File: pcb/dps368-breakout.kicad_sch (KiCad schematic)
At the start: 7 parts, among them J1 Conn_01x05_Pin, U1 DPS368XTSA1

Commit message: Removed broken property
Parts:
- U1:  Package dimensions: 8-pin LGA, 2.0 x 2.5 x 1.1 mm3 | Operat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 -> (none)
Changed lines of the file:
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@@
-      (effects (font (size 1.27 1.27)) (justify left bottom) hide)
-    )
-    (property "" "Package dimensions: 8-pin LGA, 2.0 x 2.5 x 1.1 mm3 | Operation range: Pressure: 3001200 hPa Temperature: -4085C | Precision: 0.002 hPa _or 0.02 m_ | Rel. accuracy: 0.06 hPa _or 0.5 m_ | Abs. accuracy: 1 hPa _or 8 m_ | Temperature accuracy: 0.5C | Avg. current consumption: 1.7 A_pressure measurement_ @1Hzsampling rate, standby: 0.5 A. | Integrated FIFO | Interface: I2C and SPI_both with optional interrupt_" (at 121.92 62.23 0)
       (effects (font (size 1.27 1.27)) (justify left bottom) hide)
     )

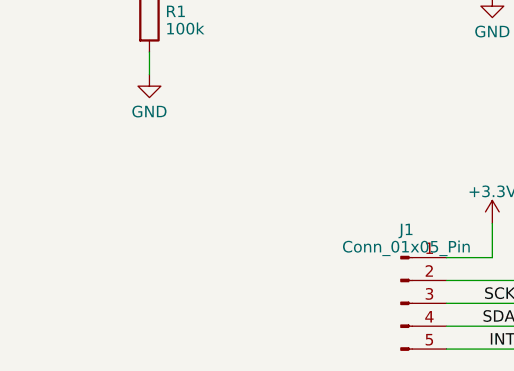
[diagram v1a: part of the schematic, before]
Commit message: Added mounting hole
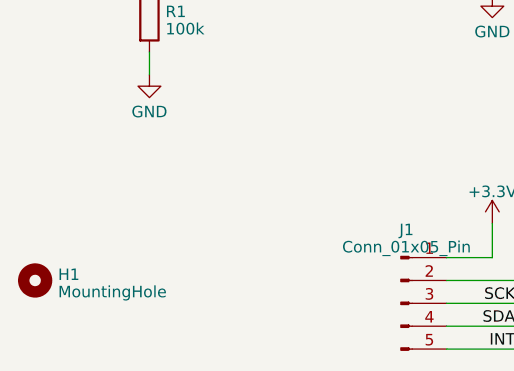
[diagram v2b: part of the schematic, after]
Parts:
- added H1: MountingHole, MountingHole:MountingHole_2.5mm_Pad_Via, symbol Mechanical:MountingHole
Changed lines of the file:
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@@
+    )
+  )
+  (symbol (lib_id "Mechanical:MountingHole") (at 88.9 104.14 0) (unit 1)
+    (in_bom yes) (on_board yes) (dnp no) (fields_autoplaced)
+    (property "Reference" "H1" (at 91.44 103.4963 0)
+      (effects (font (size 1.27 1.27)) (justify left))
+    )
+    (property "Value" "MountingHole" (at 91.44 105.4173 0)
+      (effects (font (size 1.27 1.27)) (justify left))
+    )
+    (property "Footprint" "MountingHole:MountingHole_2.5mm_Pad_Via" (at 88.9 104.14 0)
+      (effects (font (size 1.27 1.27)) hide)
+    )
+    (property "Datasheet" "~" (at 88.9 104.14 0)
+      (effects (font (size 1.27 1.27)) hide)
+    )
+    (instances
+      (project "dps368-breakout"
+        (path "/a87d30f0-0d66-475a-869d-b3a36ef9d8b3"
+          (reference "H1") (unit 1)
+        )
+      )
     )
   )
